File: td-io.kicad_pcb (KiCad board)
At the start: 2 copper layers, 200 x 76 mm, 89 parts, among them J1 USB_A, J2 USB_B, J3 JAMMA_Edge, J4 Conn_Coaxial, J5 DB15_Female_HighDensity, J6 Conn_02x04_Top_Bottom, J7 Conn_02x17_Odd_Even, J8 Conn_Coaxial, Q2 FDS6930A, Q3 FDS6930A, SW1 SW_DIP_x02, U1 LM4950TS, U10 Pico, U2 ST485EB, U3 AD813, U4 74LS86, U5 AT24CS01-SSHM, U6 74LV166, U7 TPS568230, U8 74LV166, U9 74LV166

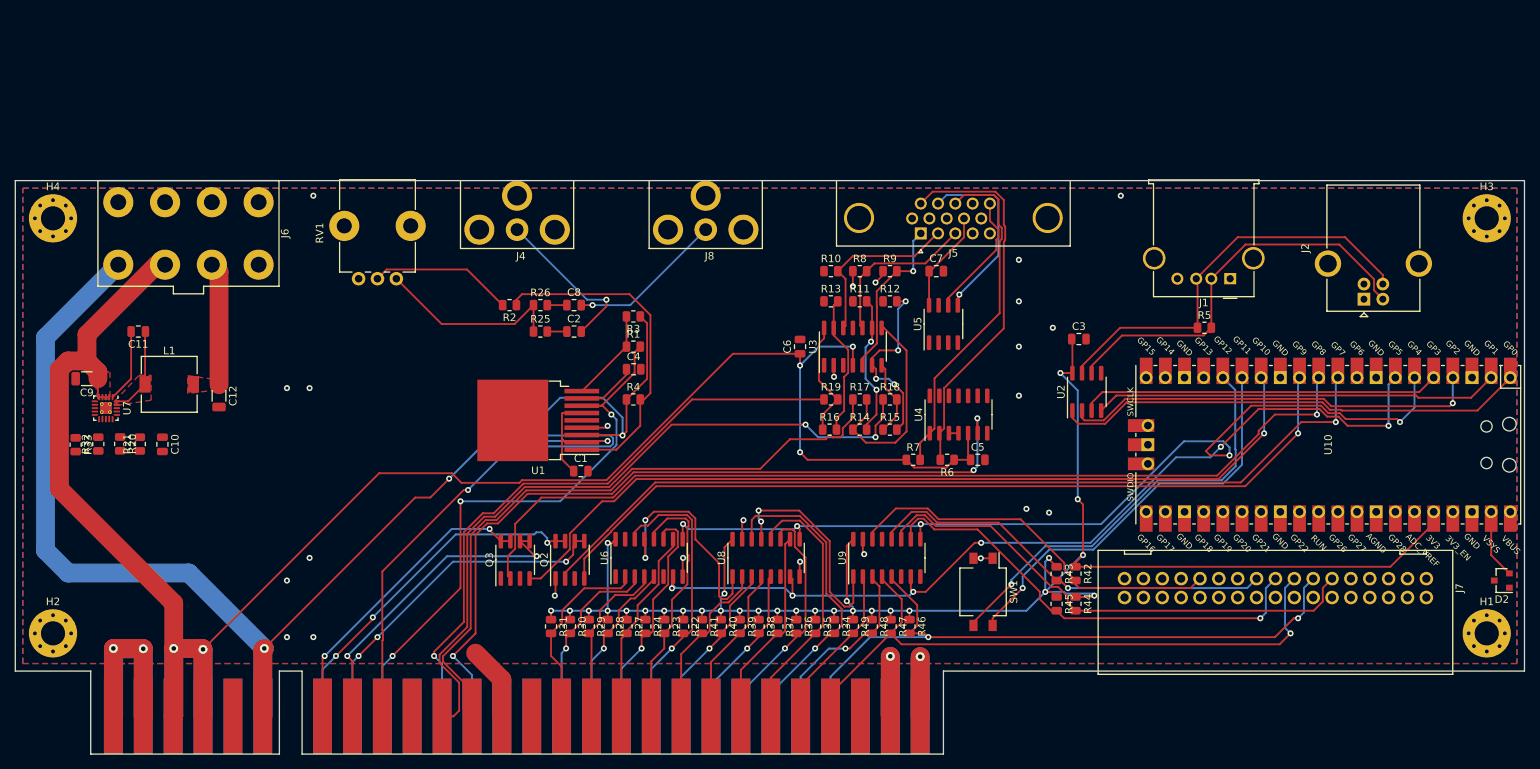
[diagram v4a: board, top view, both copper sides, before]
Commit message: More layout fixes
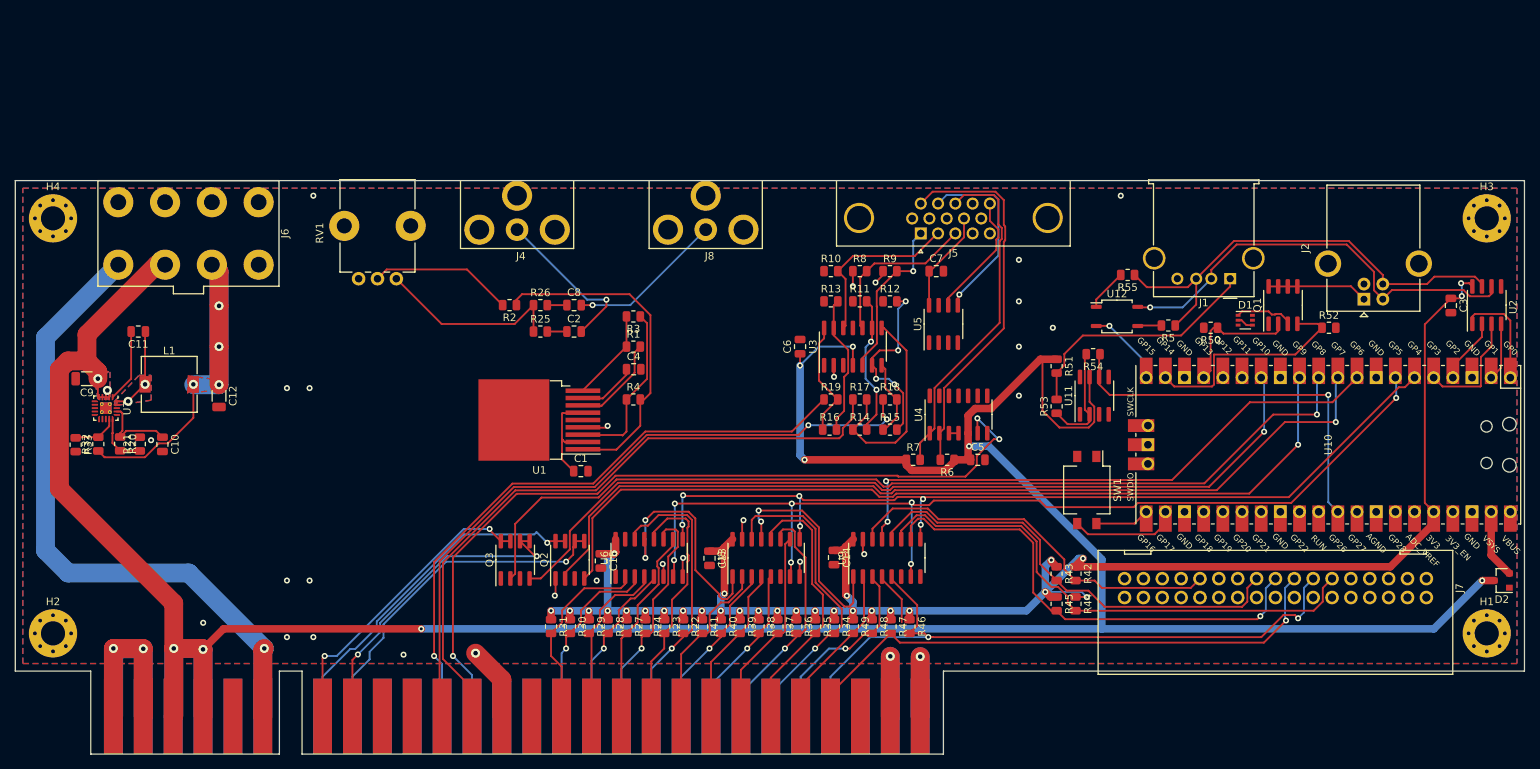
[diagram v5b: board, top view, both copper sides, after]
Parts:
- added C13: 0.1uF, Capacitor_SMD:C_0805_2012Metric, F.Cu at (164.0, 132.1)
- added C14: 0.1uF, Capacitor_SMD:C_0805_2012Metric, F.Cu at (180.5, 131.9)
- added C15: 0.1uF, Capacitor_SMD:C_0805_2012Metric, F.Cu at (149.6, 132.4)
- added D1: BAV99S, Package_TO_SOT_SMD:SOT-363_SC-70-6, F.Cu at (235.0, 100.5)
- added Q1: FDS6930B, Package_SO:SOIC-8_3.9x4.9mm_P1.27mm, F.Cu at (240.0, 98.5)
- added R50: 10k, Resistor_SMD:R_0805_2012Metric, F.Cu at (230.4, 101.5)
- added R51: 10k, Resistor_SMD:R_0805_2012Metric, F.Cu at (210.0, 106.6)
- added R52: 10k, Resistor_SMD:R_0805_2012Metric, F.Cu at (246.1, 101.5)
- added R53: 20k, Resistor_SMD:R_0805_2012Metric, F.Cu at (210.0, 111.9)
- added R54: 10k, Resistor_SMD:R_0805_2012Metric, F.Cu at (214.8, 105.0)
- added R55: R, Resistor_SMD:R_0805_2012Metric, F.Cu at (219.4, 94.5)
- added U11: TL081, Package_SO:SOIC-8_3.9x4.9mm_P1.27mm, F.Cu at (215.0, 110.5)
- added U12: CPC1017N, Package_SO:SOP-4_3.8x4.1mm_P2.54mm, F.Cu at (218.0, 100.0)
- Q2, Q3: value FDS6930A -> FDS6930B
- R1, R2, R3, R4: value R -> 20k
- RV1: footprint Potentiometer_THT:Potentiometer_Alps_RK09K_Single_Vertical -> Potentiometer_THT:Potentiometer_Bourns_PTV09A-1_Single_Vertical
- U2: value ST485EB -> SP3481CN
- moved U2 54.2 mm to (267.0, 98.5)
- moved C3 49.5 mm to (262.2, 98.5), turned to 270 degrees
- moved SW1 19.3 mm to (214.0, 123.0)
- moved R5 4.80 mm to (224.8, 101.2), turned to 180 degrees
- moved U1 0.16 mm to (141.4, 113.7)
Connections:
- net /p1select renamed Net-(J3-Pad26)
- net /p2select renamed Net-(J3-Padd)
- R5 pad 2: Net-(J1-Pad2) -> Net-(R5-Pad2)
- U10 pad 15: Net-(SW1-Pad4) -> Net-(U10-Pad15)
- U10 pad 16: Net-(SW1-Pad3) -> Net-(U10-Pad16)
- U10 pad 17: Net-(U10-Pad17) -> /sense_0v
- U10 pad 19: Net-(U10-Pad19) -> /sense_2.5v
- U10 pad 20: Net-(U10-Pad20) -> /termination
- U10 pad 21: Net-(U10-Pad21) -> Net-(SW1-Pad4)
- U10 pad 22: Net-(U10-Pad22) -> Net-(SW1-Pad3)
- U10 pad 31: Net-(U10-Pad31) -> /sense_in
- U4 pad 6: /jamma_sync -> Net-(U4-Pad6)
- U9 pad 13: Net-(U9-Pad13) -> /sr_data
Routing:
- net +5V: track 263.0 -> 414.1 mm, vias 5 -> 10
- net Net-(U4-Pad6): track 0.00 -> 107.8 mm, vias 0 -> 3
- net /jamma_sync: track 105.0 -> 0.00 mm, vias 3 -> 0
- net /speaker+: track 111.4 -> 22.9 mm, vias 2 -> 0
- net /sr_data: track 0.00 -> 76.2 mm, vias 0 -> 2
- net /speaker-: track 75.3 -> 12.6 mm, vias 3 -> 0
- net +12V: track 168.4 -> 108.3 mm, vias 4 -> 2
- net /sense_in: track 0.00 -> 51.0 mm, vias 0 -> 1
- net /jvs_rx: track 62.8 -> 14.1 mm
- net Net-(SW1-Pad4): track 54.9 -> 7.25 mm, vias 1 -> 0
- net /jvs_re: track 55.4 -> 8.73 mm, vias 1 -> 0
- net /jvs_tx: track 53.7 -> 7.68 mm
- net Net-(SW1-Pad3): track 56.5 -> 14.4 mm, vias 1 -> 0
- net +3.3VP: track 16.3 -> 55.5 mm, vias 0 -> 4
- net Net-(J1-Pad1): track 0.00 -> 33.2 mm
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- added copper zone on B.Cu, net (none)
- added copper zone on F.Cu, net +3.3VP
- removed copper zone on F.Cu, net +3V3

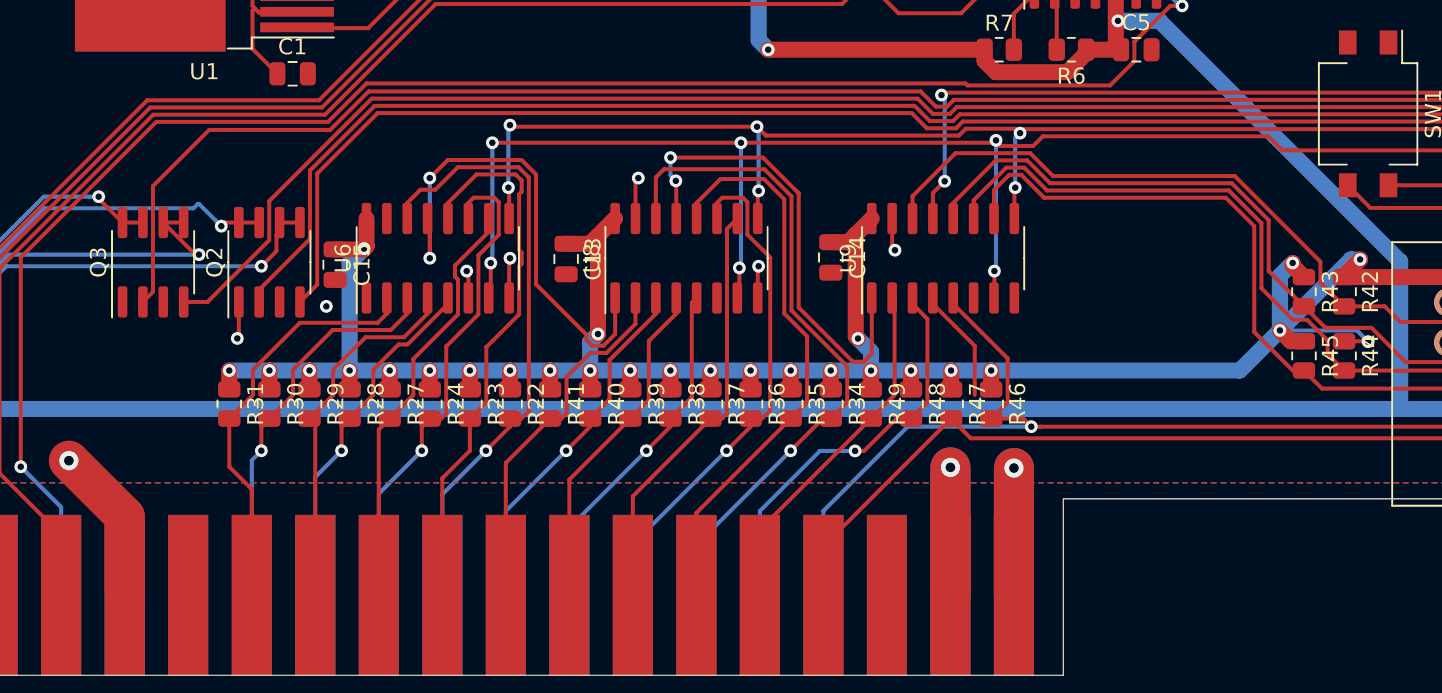
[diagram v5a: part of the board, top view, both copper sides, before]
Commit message: Add service/test/tilt
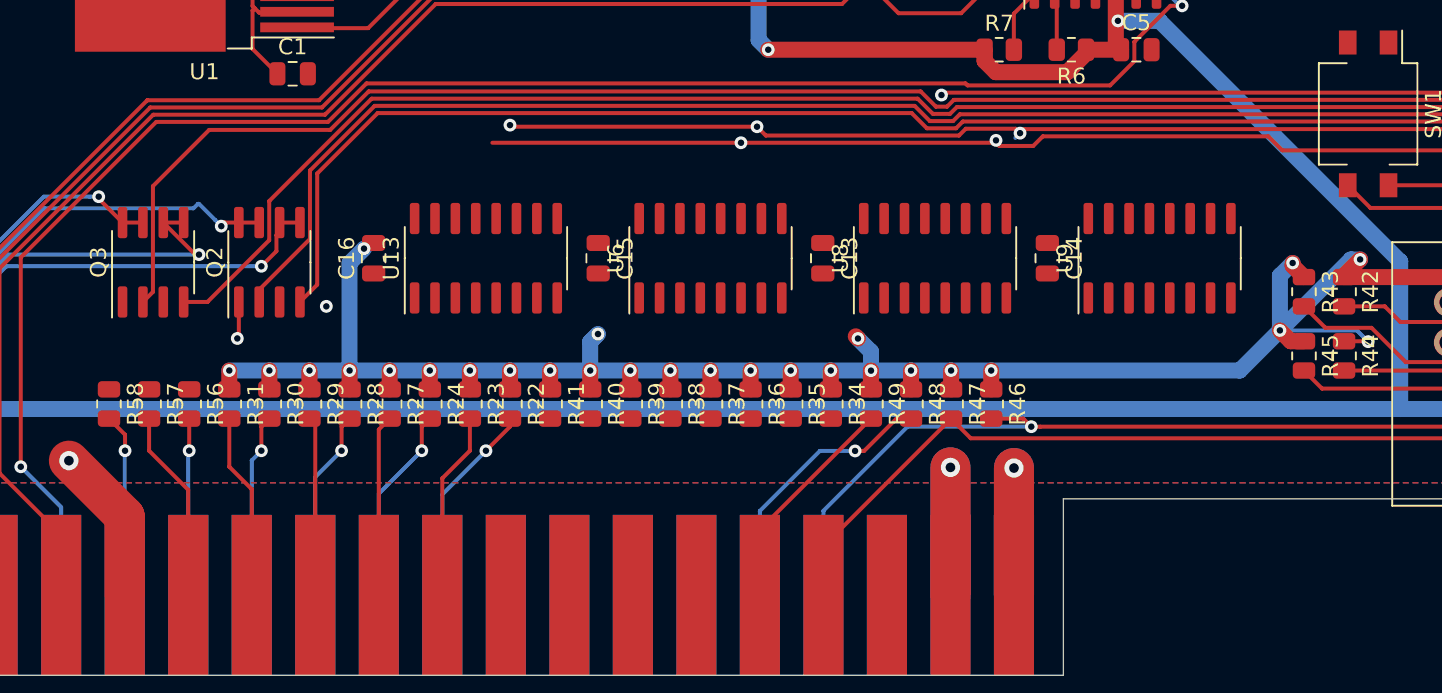
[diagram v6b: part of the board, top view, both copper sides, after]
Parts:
- added C16: 0.1uF, Capacitor_SMD:C_0805_2012Metric, F.Cu at (152.0, 132.0)
- added R56: 10k, Resistor_SMD:R_0805_2012Metric, F.Cu at (140.5, 141.1)
- added R57: 10k, Resistor_SMD:R_0805_2012Metric, F.Cu at (138.0, 141.1)
- added R58: 10k, Resistor_SMD:R_0805_2012Metric, F.Cu at (135.5, 141.1)
- added U13: 74LS165, Package_SO:SOIC-16_3.9x9.9mm_P1.27mm, F.Cu at (159.0, 132.0)
- U6, U8, U9: value 74LV166 -> 74LS165
- moved U6 17.0 mm to (173.0, 132.0)
- moved C15 16.4 mm to (166.0, 132.0)
- moved C13 16.0 mm to (180.0, 132.0)
- moved U8 15.5 mm to (187.0, 132.0)
- moved C14 13.5 mm to (194.0, 132.0)
- moved U9 13.5 mm to (201.0, 132.0)
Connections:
- J3 pad 15: Net-(J3-Pad15) -> /test
- J3 pad R: Net-(J3-PadR) -> /service
- J3 pad S: Net-(J3-PadS) -> /tilt
- U6 pad 1: GND -> /sr_clr
- U6 pad 10: /p1up -> Net-(U13-Pad9)
- U6 pad 11: /p2up -> /c1
- U6 pad 12: /p1down -> /c2
- U6 pad 13: Net-(U6-Pad13) -> /p1start
- U6 pad 14: /p2down -> /p2start
- U6 pad 2: /c1 -> /sr_clk
- U6 pad 3: /c2 -> /p1up
- U6 pad 4: /p1start -> /p2up
- U6 pad 5: /p2start -> /p1down
- U6 pad 6: GND -> /p2down
- U6 pad 7: /sr_clk -> Net-(U6-Pad7)
- U6 pad 9: /sr_clr -> Net-(U6-Pad9)
- U8 pad 1: Net-(U6-Pad13) -> /sr_clr
- U8 pad 10: /p1_1 -> Net-(U6-Pad9)
- U8 pad 11: /p2_1 -> /p1left
- U8 pad 12: /p1_2 -> /p2left
- U8 pad 13: Net-(U8-Pad13) -> /p1right
- U8 pad 14: /p2_2 -> /p2right
- U8 pad 2: /p1left -> /sr_clk
- U8 pad 3: /p2left -> /p1_1
- U8 pad 4: /p1right -> /p2_1
- U8 pad 5: /p2right -> /p1_2
- U8 pad 6: GND -> /p2_2
- U8 pad 7: /sr_clk -> Net-(U8-Pad7)
- U8 pad 9: /sr_clr -> Net-(U8-Pad9)
- U9 pad 1: Net-(U8-Pad13) -> /sr_clr
- U9 pad 10: /p1_5 -> Net-(U8-Pad9)
- U9 pad 11: /p2_5 -> /p1_3
- U9 pad 12: /p1_6 -> /p2_3
- U9 pad 13: /sr_data -> /p1_4
- U9 pad 14: /p2_6 -> /p2_4
- U9 pad 2: /p1_3 -> /sr_clk
- U9 pad 3: /p2_3 -> /p1_5
- U9 pad 4: /p1_4 -> /p2_5
- U9 pad 5: /p2_4 -> /p1_6
- U9 pad 6: GND -> /p2_6
- U9 pad 7: /sr_clk -> Net-(U9-Pad7)
- U9 pad 9: /sr_clr -> /sr_data
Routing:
- net /p2_2: track 42.4 -> 0.00 mm, vias 1 -> 0
- net /p1_2: track 35.7 -> 0.00 mm
- net /p2_6: track 51.5 -> 17.4 mm
- net /p2_5: track 70.0 -> 36.8 mm
- net /p2_1: track 32.2 -> 0.00 mm, vias 1 -> 0
- net Net-(U6-Pad13): track 31.1 -> 0.00 mm, vias 2 -> 0
- net /p1_5: track 63.8 -> 33.4 mm
- net Net-(U8-Pad13): track 29.6 -> 0.00 mm, vias 2 -> 0
- net /p1_6: track 60.1 -> 30.5 mm
- net /sr_clk: track 134.7 -> 105.2 mm, vias 7 -> 3
- net /p1_1: track 26.6 -> 0.00 mm
- net /p2down: track 38.4 -> 12.7 mm
- net +3V3: track 236.1 -> 212.7 mm
- net /p1left: track 22.9 -> 0.00 mm
- net /p1down: track 34.5 -> 11.7 mm
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
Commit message: more layout
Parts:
- removed R2, R3, R4: 20k, Resistor_SMD:R_0805_2012Metric
- added C17: 100uF, Capacitor_SMD:C_1206_3216Metric, F.Cu at (159.0, 100.5)
- added C18: 100uF, Capacitor_SMD:C_1206_3216Metric, F.Cu at (143.8, 100.5)
- added C19: 1uF, Capacitor_SMD:C_0805_2012Metric, F.Cu at (168.9, 116.0)
- added C20: 1uF, Capacitor_SMD:C_0805_2012Metric, F.Cu at (148.9, 116.0)
- added C21: 1uF, Capacitor_SMD:C_0805_2012Metric, F.Cu at (146.9, 93.0)
- added C22: 1uF, Capacitor_SMD:C_0805_2012Metric, F.Cu at (153.1, 116.0)
- added C23: 1uF, Capacitor_SMD:C_0805_2012Metric, F.Cu at (133.1, 116.0)
- added C24: 2.2uF, Capacitor_SMD:C_0805_2012Metric, F.Cu at (165.1, 116.0)
- added C25: 2.2uF, Capacitor_SMD:C_0805_2012Metric, F.Cu at (156.9, 116.0)
- added C26: 2.2uF, Capacitor_SMD:C_0805_2012Metric, F.Cu at (145.1, 116.0)
- added C27: 2.2uF, Capacitor_SMD:C_0805_2012Metric, F.Cu at (136.9, 116.0)
- added J9: Conn_01x04_Male, Connector_JST:JST_EH_B4B-EH-A_1x04_P2.50mm_Vertical, F.Cu at (147.5, 120.0)
- added L2: 15uH, Inductor_SMD:L_7.3x7.3_H4.5, F.Cu at (166.0, 110.0)
- added L3: 15uH, Inductor_SMD:L_7.3x7.3_H4.5, F.Cu at (156.0, 110.0)
- added L4: 15uH, Inductor_SMD:L_7.3x7.3_H4.5, F.Cu at (146.0, 110.0)
- added L5: 15uH, Inductor_SMD:L_7.3x7.3_H4.5, F.Cu at (136.0, 110.0)
- added SW2: SW_DIP_x01, Button_Switch_SMD:SW_DIP_SPSTx01_Slide_Omron_A6S-110x_W8.9mm_P2.54mm, F.Cu at (119.5, 103.0)
- C1: value 0.1uF -> 1uF
- C4: value 10uF -> 1uF
- Q2, Q3: value FDS6930B -> ZXMS6004DN8
- R1: value 20k -> 10k
- RV1: value 10k Audio -> R_POT_Dual; footprint Potentiometer_THT:Potentiometer_Bourns_PTV09A-1_Single_Vertical -> td-io:PTV112-4420A-A503
- U1: value LM4950TS -> TPA3138D2; footprint Package_TO_SOT_SMD:TO-263-9_TabPin5 -> Package_SO:HTSSOP-28-1EP_4.4x9.7mm_P0.65mm_EP2.85x5.4mm_ThermalVias
- U3: value AD813 -> ADA4891-3
- moved C1 27.8 mm to (151.1, 93.0)
- moved C2 24.2 mm to (124.5, 113.0)
- moved C8 24.2 mm to (124.5, 109.5)
- moved R25 24.2 mm to (120.1, 113.0)
- moved R26 24.2 mm to (120.1, 109.5)
- moved C4 17.7 mm to (143.1, 93.0)
- moved U1 17.0 mm to (151.5, 100.0), turned to 270 degrees
- moved R1 11.0 mm to (154.9, 93.0), turned to 180 degrees
- moved RV1 7.91 mm to (120.0, 87.5), turned to 0 degrees
- moved C13 0.50 mm to (180.5, 132.0)
- moved C14 0.50 mm to (194.5, 132.0)
- moved C15 0.50 mm to (166.5, 132.0)
- moved C16 0.50 mm to (152.5, 132.0), turned to 270 degrees
- moved Q3 0.10 mm to (138.2, 132.3)
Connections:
- C1 pad 1: +12V -> GND
- C1 pad 2: GND -> Net-(C1-Pad2)
- C4 pad 1: Net-(C4-Pad1) -> GND
- C4 pad 2: GND -> Net-(C4-Pad2)
- J3 pad 5: -5V -> Net-(J3-Pad5)
- J3 pad E: -5V -> Net-(J3-PadE)
- R1 pad 2: /speaker- -> +12V
- R26 pad 1: Net-(R25-Pad1) -> Net-(R26-Pad1)
- RV1 pad 2: Net-(R2-Pad2) -> Net-(RV1-Pad2)
- U1 pad 2: +12V -> Net-(R1-Pad1)
- U1 pad 3: /speaker+ -> Net-(RV1-Pad2)
- U1 pad 4: GND -> Net-(C1-Pad2)
- U1 pad 6: +12V -> GND
- U1 pad 7: /speaker- -> +12V
- U1 pad 8: Net-(C4-Pad1) -> GND
- U1 pad 9: Net-(R1-Pad1) -> Net-(C21-Pad2)
- U4 pad 6: Net-(U4-Pad6) -> /jamma_sync
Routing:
- net Net-(U4-Pad6): track 107.8 -> 0.00 mm, vias 3 -> 0
- net /jamma_sync: track 0.00 -> 107.5 mm, vias 0 -> 3
- net +12V: track 108.3 -> 210.3 mm, vias 2 -> 6
- net +3V3: track 212.7 -> 283.9 mm, vias 29 -> 38
- net /speaker-: track 12.6 -> 64.9 mm, vias 0 -> 2
- net /speaker+: track 22.9 -> 75.0 mm
- net /p1left: track 0.00 -> 49.3 mm
- net /p2left: track 0.00 -> 46.8 mm, vias 0 -> 1
- net Net-(U1-Pad1): track 44.5 -> 0.00 mm
- net /c1: track 11.6 -> 54.9 mm
- net /p1right: track 0.00 -> 42.0 mm
- net /sr_clr: track 104.9 -> 146.6 mm, vias 3 -> 8
- net Net-(RV1-Pad2): track 0.00 -> 41.6 mm, vias 0 -> 2
- net Net-(RV1-Pad5): track 0.00 -> 40.9 mm, vias 0 -> 2
- net /sr_clk: track 105.2 -> 144.9 mm, vias 3 -> 8
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- added copper zone on F.Cu, net Net-(L2-Pad1)
- added copper zone on F.Cu, net Net-(L3-Pad1)
- added copper zone on F.Cu, net Net-(L4-Pad1)
- added copper zone on F.Cu, net Net-(L5-Pad1)
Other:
- board text added: "+"
- board text added: "-"
- board text added: "L"
- board text added: "R"
- board text added: "mono"
- board text added: "stereo"

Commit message: More PCB layout
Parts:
- J5: footprint Connector_Dsub:DSUB-15-HD_Female_Horizontal_P2.29x1.98mm_EdgePinOffset3.03mm_Housed_MountingHolesOffset4.94mm -> Connector_Dsub:DSUB-15-HD_Female_Horizontal_P2.29x1.98mm_EdgePinOffset8.35mm_Housed_MountingHolesOffset10.89mm
- U10: footprint MCU_RaspberryPi_and_Boards:RPi_Pico_SMD_TH -> td-io:RPi_Pico_SMD
- moved C7 12.1 mm to (190.5, 105.5), turned to 270 degrees
- moved J5 5.42 mm to (192.2, 94.4)
- moved R10 4.53 mm to (179.6, 98.5)
- moved R8 4.53 mm to (183.4, 98.5)
- moved R9 4.53 mm to (187.4, 98.5)
- moved U5 4.50 mm to (195.0, 105.5)
- moved C6 4.03 mm to (175.5, 108.0)
- moved R11 4.03 mm to (183.4, 102.0)
- moved R12 4.03 mm to (187.4, 102.0)
- moved R13 4.03 mm to (179.6, 102.0)
- moved R14 4.03 mm to (183.4, 119.0)
- moved R15 4.03 mm to (187.4, 119.0)
- moved R16 4.03 mm to (179.4, 119.0)
- moved R17 4.03 mm to (183.4, 115.0)
- moved R18 4.03 mm to (187.4, 115.0)
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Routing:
- net GND: track 104.9 -> 112.0 mm, vias 58 -> 64
- net +5V: track 420.0 -> 414.8 mm, vias 9 -> 10
- net /vga_hsync: track 45.6 -> 41.7 mm
- net +12V: track 210.3 -> 207.4 mm
- net /jamma_blue: track 86.6 -> 83.8 mm
- net /vga_vsync: track 50.3 -> 47.6 mm
- net Net-(C7-Pad1): track 13.5 -> 15.8 mm
- net +3V3: track 283.9 -> 286.2 mm
- net /p1_4: track 98.0 -> 100.2 mm
- net /jamma_red: track 90.3 -> 88.2 mm
- net /jamma_green: track 80.9 -> 78.8 mm
- net /vga_red: track 22.0 -> 20.4 mm
- net /speaker-: track 64.9 -> 66.3 mm
- net /p2_2: track 29.1 -> 30.6 mm
- net /p2_1: track 29.9 -> 31.4 mm
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- added copper zone on B.Cu, net +5V
- added copper zone on B.Cu, net /SW
- removed copper zone on B.Cu, net (none)
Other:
- board size 200 x 76 mm -> 200 x 75 mm
- board text added: "td-io v1.0 2021 https://github.com/tdaede/td-io CERN-OHL-W"
